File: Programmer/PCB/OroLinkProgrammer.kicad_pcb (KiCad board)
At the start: 2 copper layers, 77.6 x 54.9 mm, 14 parts, among them IC1 SE555DR, J1 67996-110HLF, M1 STM32 STLINK V3MODS

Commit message: add keepout area around bottom mounting hole
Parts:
- moved R3 2.31 mm to (142.0, 102.9), turned to 0 degrees
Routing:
- net /VCC: track 41.4 -> 32.8 mm, vias 0 -> 2
- net Net-(IC1-THRES): track 24.1 -> 18.0 mm
- net Net-(IC1-DISCH): track 24.7 -> 25.5 mm
- net GND: track 27.0 -> 27.6 mm, vias 15 -> 13

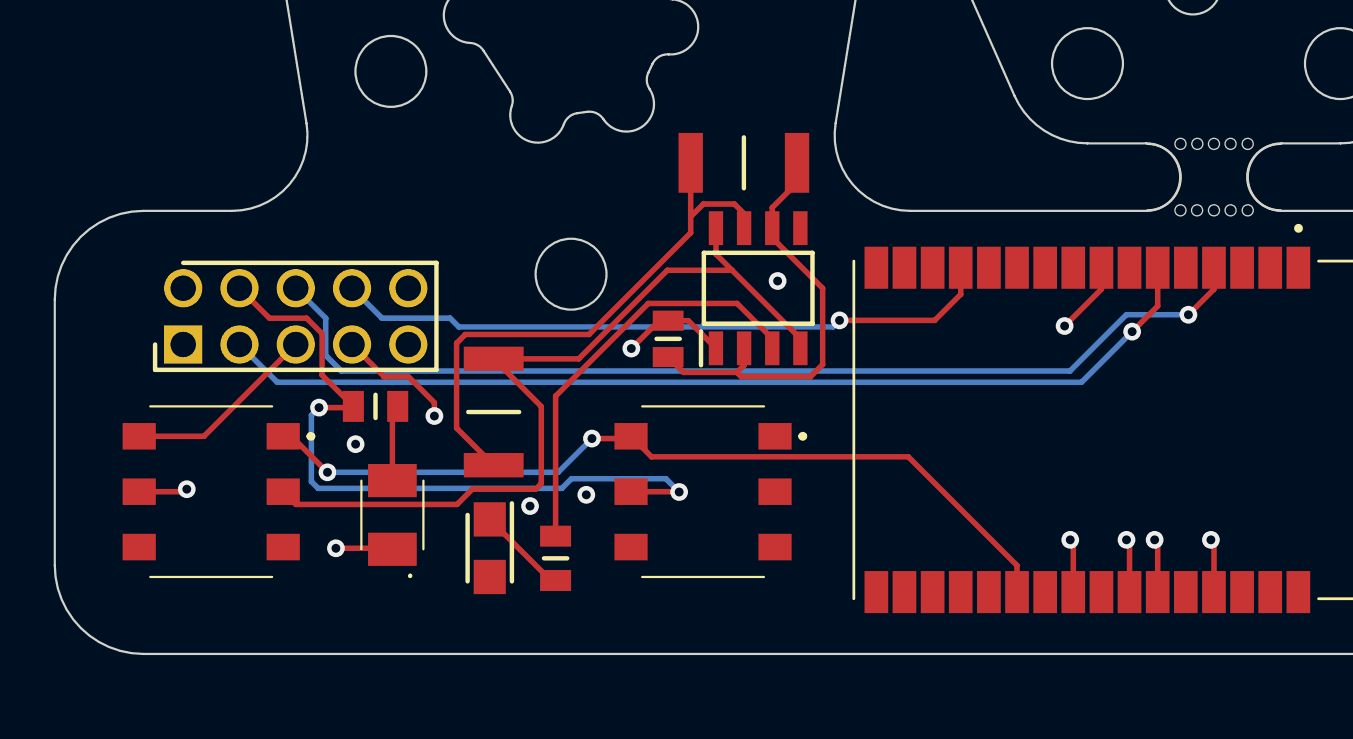
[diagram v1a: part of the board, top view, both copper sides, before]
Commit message: swap switch position and bring high resistor down into more suitable position
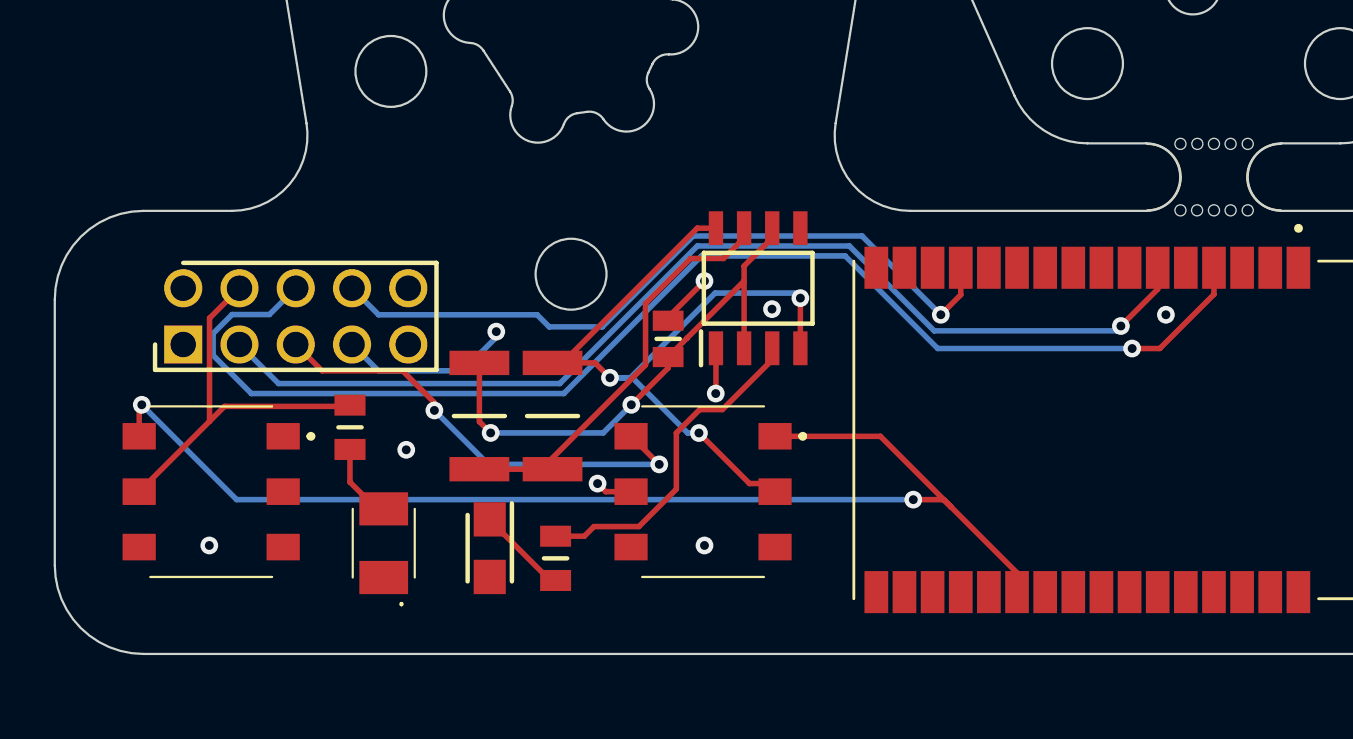
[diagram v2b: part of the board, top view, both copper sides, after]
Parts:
- moved S1 22.2 mm to (117.9, 117.7)
- moved S2 22.2 mm to (140.1, 117.7)
- moved R3 16.5 mm to (130.0, 114.3), turned to 90 degrees
- moved R2 2.66 mm to (133.3, 114.3)
- moved R1 1.49 mm to (124.2, 114.8), turned to -90 degrees
- moved LED1 1.33 mm to (125.7, 120.0)
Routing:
- net +5V: track 37.6 -> 54.3 mm
- net /VCC: track 32.8 -> 17.6 mm, vias 2 -> 0
- net GND: track 27.6 -> 13.9 mm, vias 13 -> 9
- net /FLASH: track 8.78 -> 20.6 mm, vias 0 -> 2
- net /SWDIO: track 46.5 -> 58.0 mm
- net Net-(IC1-DISCH): track 25.5 -> 18.4 mm
- net Net-(IC1-THRES): track 18.0 -> 23.5 mm, vias 0 -> 2
- net Net-(IC1-OUT): track 18.5 -> 14.6 mm
- net Net-(IC1-RESET): track 37.8 -> 34.4 mm, vias 0 -> 3
- net /SWCLK: track 30.0 -> 33.0 mm
- net /SWO: track 45.3 -> 48.1 mm
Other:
- board text added: "STENCIL DIMENSIONS"

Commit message: add silkscreens and tweak a via
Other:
- board text added: "FLASH"
- board text added: "ORO OPERATING SYSTEM オロ オペレーティング システム oro programmer rev.1 2023-05-13 oro.sh"
- board text added: "PWR"

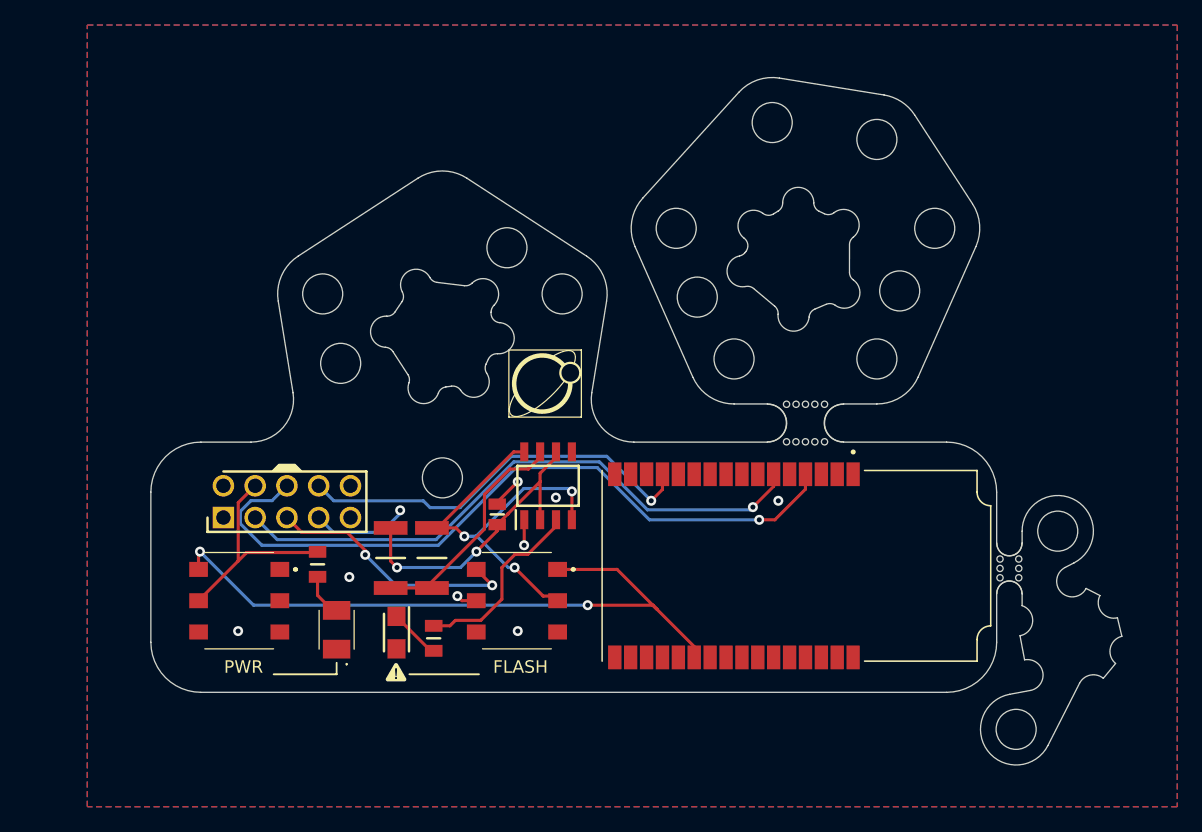
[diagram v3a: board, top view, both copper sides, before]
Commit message: add second brace to board and reduce ground fill
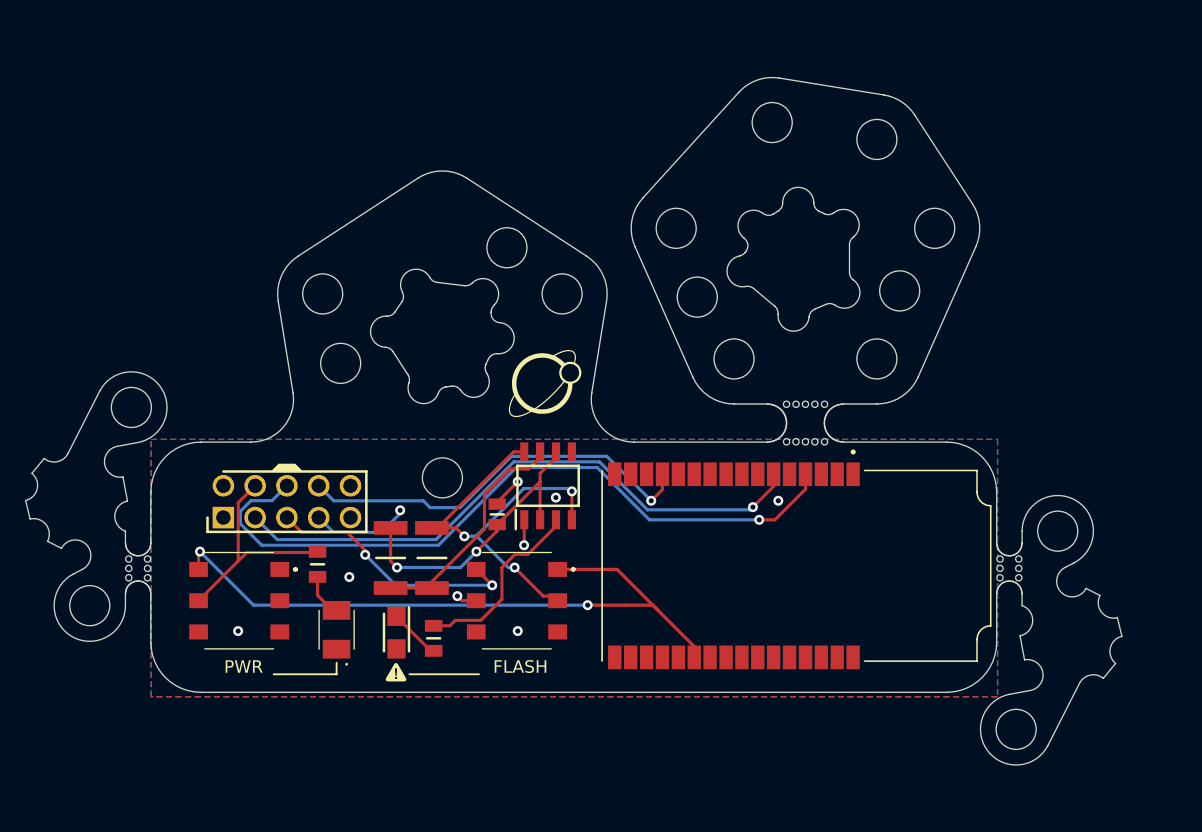
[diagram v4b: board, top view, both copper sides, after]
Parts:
- added mouse-bite-2mm-slot: VAL**, panelization:mouse-bite-2mm-slot, F.Cu at (109.9, 115.1)
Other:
- board size 77.6 x 54.9 mm -> 87.6 x 54.9 mm

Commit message: layout of new programmer revision
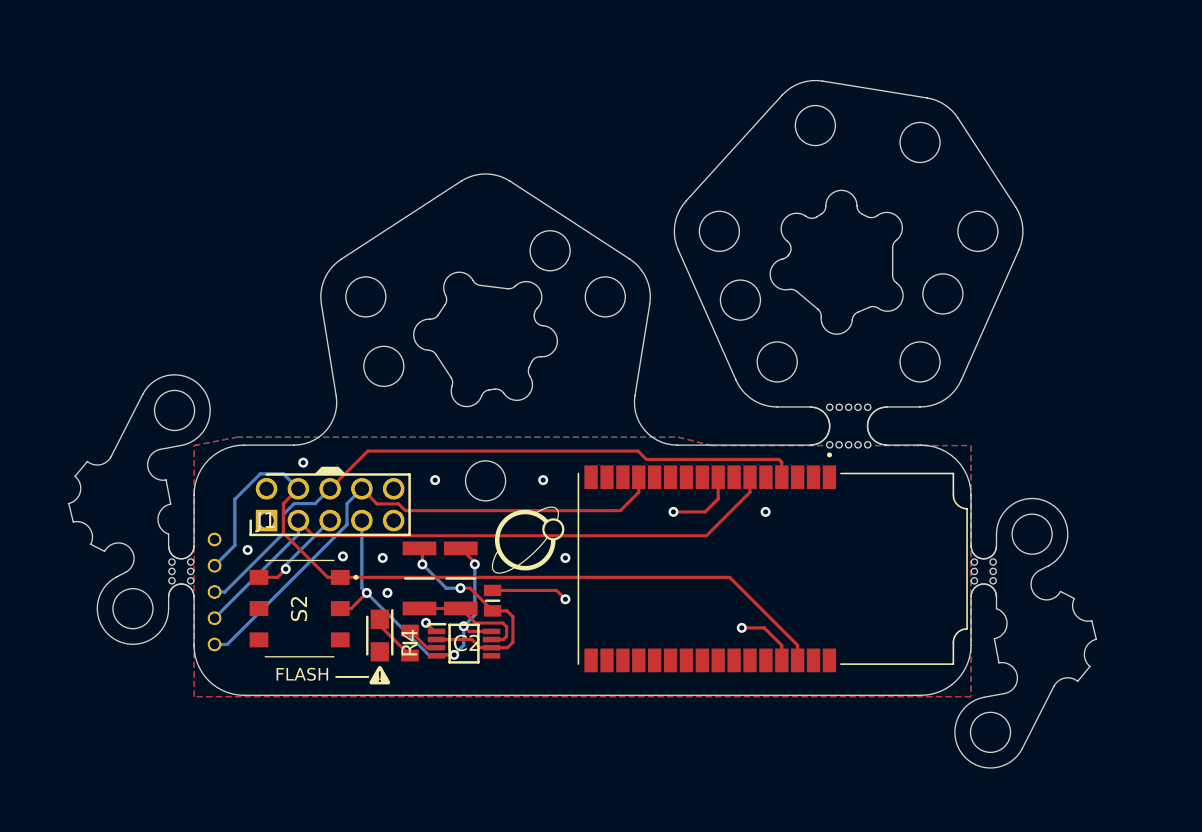
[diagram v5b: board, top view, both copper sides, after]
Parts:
- removed IC1: SE555DR, SamacSys_Parts:SOIC127P600X175-8N
- removed LED1: AA3528VRVFS/A, SamacSys_Parts:AA3528VRVFSA
- removed R1: 1k, SamacSys_Parts:RESC2012X60N
- removed S1: 452403012014, SamacSys_Parts:452403012014
- added DBG1: ~, Oro Footprints:DebugPin, F.Cu at (116.0, 114.9)
- added DBG2: ~, Oro Footprints:DebugPin, F.Cu at (116.0, 117.0)
- added DBG3: ~, Oro Footprints:DebugPin, F.Cu at (116.0, 121.2)
- added DBG4: ~, Oro Footprints:DebugPin, F.Cu at (116.0, 119.1)
- added DBG5: ~, Oro Footprints:DebugPin, F.Cu at (116.0, 112.8)
- added IC2: LMC555CMMX_NOPB, SamacSys_Parts:SOP65P490X110-8N, F.Cu at (135.9, 121.1)
- moved S2 17.4 mm to (122.8, 118.4)
- moved C1 6.91 mm to (138.2, 117.7)
- moved mouse-bite-2mm-slot 3.46 mm to (113.3, 115.4)
- moved mouse-bite-3mm-slot 3.46 mm to (166.7, 103.8)
- moved J1 3.46 mm to (120.1, 111.3)
- moved R2 2.83 mm to (135.7, 115.9)
- moved R3 2.83 mm to (132.4, 115.9)
- moved mouse-bite-2mm-slot 2.06 mm to (177.5, 115.4)
- moved R4 1.93 mm to (131.6, 121.1)
- moved M1 1.91 mm to (176.3, 106.7)
- moved LED2 1.36 mm to (129.2, 120.5)
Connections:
- net /FLASH renamed /BOOT0
- J1 pad 4: /VCC -> /VREF
- J1 pad 7: GND -> /BOOT1
- M1 pad 22: +5V -> unconnected-(M1-5V_200A-Pad22)
- M1 pad 30: unconnected-(M1-VCC-Pad30) -> /VREF
- M1 pad 31: unconnected-(M1-NRST-Pad31) -> GND
- R2 pad 1: Net-(IC1-RESET) -> /BOOT1
- S2 pad 1: +5V -> /VREF
- S2 pad 2: Net-(IC1-RESET) -> /BOOT1
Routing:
- net /VREF: track 0.00 -> 62.4 mm
- net +5V: track 54.3 -> 0.00 mm, vias 2 -> 0
- net Net-(IC1-RESET): track 34.4 -> 0.00 mm, vias 3 -> 0
- net /BOOT1: track 0.00 -> 31.0 mm, vias 0 -> 4
- net /VCC: track 17.6 -> 0.00 mm
- net /BOOT0: track 20.6 -> 7.76 mm, vias 2 -> 1
- net Net-(IC2-OUTPUT): track 14.6 -> 2.68 mm
- net /SWCLK: track 33.0 -> 42.6 mm, vias 1 -> 0
- net Net-(IC2-DISCHARGE): track 18.4 -> 9.64 mm
- net /SWDIO: track 58.0 -> 52.5 mm, vias 1 -> 0
- net Net-(IC2-THRESHOLD): track 23.5 -> 18.6 mm
- net GND: track 13.9 -> 17.8 mm, vias 9 -> 13
- net Net-(LED1-Pad2): track 3.18 -> 0.00 mm
- net /SWO: track 48.1 -> 49.8 mm, vias 1 -> 0
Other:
- board size 87.6 x 54.9 mm -> 82.1 x 54.9 mm
- board text removed: "PWR"
- board text removed: "STENCIL DIMENSIONS"
